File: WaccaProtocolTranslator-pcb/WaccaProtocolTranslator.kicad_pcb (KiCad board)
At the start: 2 copper layers, 161.5 x 111 mm, 114 parts, among them IC1 W25Q16JVUXIQ_TR, IC2 W25Q16JVUXIQ_TR, J1 USB_C_Receptacle_USB2.0, J10 Barrel_Jack, J2 6116314-1, J3 USB_C_Receptacle_USB2.0, J4 USB_C_Receptacle_USB2.0, J5 Conn_01x03_Male, J6 Conn_01x03_Male, J7 Conn_02x02_Odd_Even, J8 Conn_01x08_Male, J9 Barrel_Jack, Q1 IRLB8721PBF, Q2 IRLB8721PBF, SW1 Program Left, SW2 Program Right, SW3 Reset, U1 NCP1117-3.3_SOT223, U2 93LCxxB, U3 RP2040, U4 FT232HQ-REEL, U5 RP2040, Y1 ABLS-12.000MHZ-B4-T, Y2 ABLS-12.000MHZ-B4-T, Y3 ABLS-12.000MHZ-B4-T

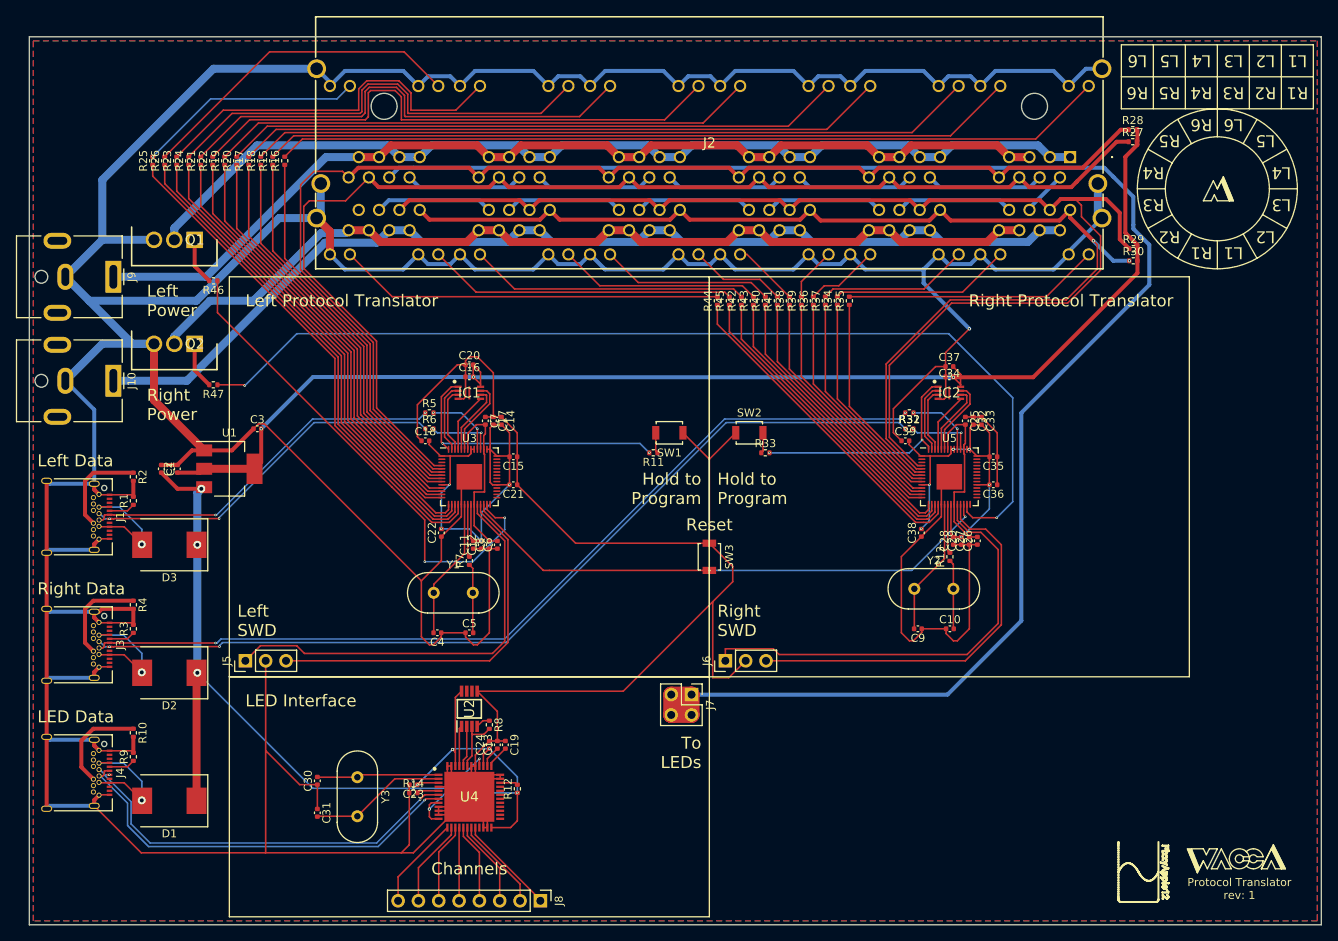
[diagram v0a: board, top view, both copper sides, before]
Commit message: A few changes that needed to be pushed, the power switching circuitry has been removed temporarily to allow for manual power switching. I also baked the FT232HQ connection to the LED bus and changed the Via sizes to match the drilling specs required by most PCB fab services.
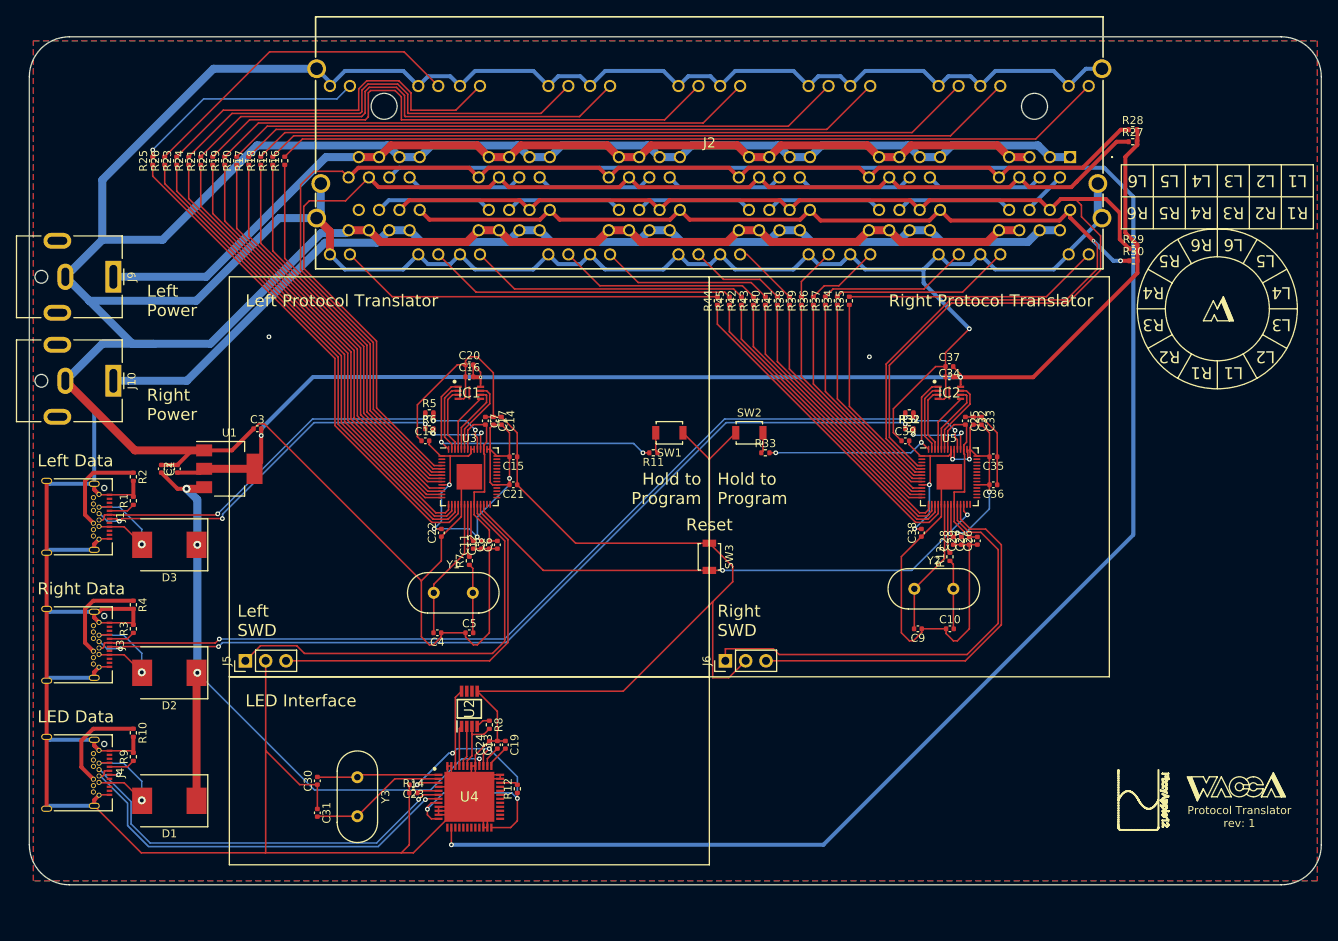
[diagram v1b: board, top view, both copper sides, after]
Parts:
- removed J7: Conn_02x02_Odd_Even, Connector_PinHeader_2.54mm:PinHeader_2x02_P2.54mm_Vertical
- removed J8: Conn_01x08_Male, Connector_PinHeader_2.54mm:PinHeader_1x08_P2.54mm_Vertical
- removed Q1, Q2: IRLB8721PBF, SamacSys_Parts:TO254P483X1016X1994-3P
- removed R46, R47: 275, Resistor_SMD:R_0402_1005Metric
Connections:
- C1 pad 1: Earth -> TP_GND_LEFT
- C10 pad 1: Earth -> TP_GND_LEFT
- C11 pad 1: Earth -> TP_GND_LEFT
- C12 pad 1: Earth -> TP_GND_LEFT
- C13 pad 2: Earth -> TP_GND_LEFT
- C14 pad 1: Earth -> TP_GND_LEFT
- C15 pad 1: Earth -> TP_GND_LEFT
- C16 pad 1: Earth -> TP_GND_LEFT
- C17 pad 1: Earth -> TP_GND_LEFT
- C18 pad 1: Earth -> TP_GND_LEFT
- C19 pad 1: Earth -> TP_GND_LEFT
- C2 pad 2: Earth -> TP_GND_LEFT
- C20 pad 1: Earth -> TP_GND_LEFT
- C21 pad 1: Earth -> TP_GND_LEFT
- C22 pad 1: Earth -> TP_GND_LEFT
- C23 pad 2: Earth -> TP_GND_LEFT
- C24 pad 2: Earth -> TP_GND_LEFT
- C25 pad 1: Earth -> TP_GND_LEFT
- C26 pad 1: Earth -> TP_GND_LEFT
- C27 pad 1: Earth -> TP_GND_LEFT
- C28 pad 1: Earth -> TP_GND_LEFT
- C29 pad 1: Earth -> TP_GND_LEFT
- C3 pad 1: Earth -> TP_GND_LEFT
- C30 pad 1: Earth -> TP_GND_LEFT
- C31 pad 1: Earth -> TP_GND_LEFT
- C32 pad 1: Earth -> TP_GND_LEFT
- C33 pad 1: Earth -> TP_GND_LEFT
- C34 pad 1: Earth -> TP_GND_LEFT
- C35 pad 1: Earth -> TP_GND_LEFT
- C36 pad 1: Earth -> TP_GND_LEFT
- C37 pad 1: Earth -> TP_GND_LEFT
- C38 pad 1: Earth -> TP_GND_LEFT
- C39 pad 1: Earth -> TP_GND_LEFT
- C4 pad 1: Earth -> TP_GND_LEFT
- C5 pad 1: Earth -> TP_GND_LEFT
- C6 pad 1: Earth -> TP_GND_LEFT
- C7 pad 1: Earth -> TP_GND_LEFT
- C8 pad 1: Earth -> TP_GND_LEFT
- C9 pad 1: Earth -> TP_GND_LEFT
- IC1 pad 4: Earth -> TP_GND_LEFT
- IC2 pad 4: Earth -> TP_GND_LEFT
- J1 pad A1: Earth -> TP_GND_LEFT
- J1 pad A12: Earth -> TP_GND_LEFT
- J1 pad B1: Earth -> TP_GND_LEFT
- J1 pad B12: Earth -> TP_GND_LEFT
- J1 pad S1: Earth -> TP_GND_LEFT
- J10 pad 2: Earth -> TP_GND_LEFT
- J2 pad A10: Earth -> TP_GND_LEFT
- J2 pad A12: Earth -> TP_GND_LEFT
- J2 pad B10: Earth -> TP_GND_LEFT
- J2 pad B12: Earth -> TP_GND_LEFT
- J2 pad C10: Earth -> TP_GND_LEFT
- J2 pad C12: Earth -> TP_GND_LEFT
- J2 pad D10: Earth -> TP_GND_LEFT
- J2 pad D12: Earth -> TP_GND_LEFT
- J2 pad E10: Earth -> TP_GND_LEFT
- J2 pad E12: Earth -> TP_GND_LEFT
- J2 pad F10: Earth -> TP_GND_LEFT
- J2 pad F12: Earth -> TP_GND_LEFT
- J2 pad G1: TP_GND_RIGHT -> TP_GND_LEFT
- J2 pad G11: Earth -> TP_GND_LEFT
- J2 pad G3: TP_GND_RIGHT -> TP_GND_LEFT
- J2 pad G9: Earth -> TP_GND_LEFT
- J2 pad H1: TP_GND_RIGHT -> TP_GND_LEFT
- J2 pad H11: Earth -> TP_GND_LEFT
- J2 pad H3: TP_GND_RIGHT -> TP_GND_LEFT
- J2 pad H9: Earth -> TP_GND_LEFT
- J2 pad J1: TP_GND_RIGHT -> TP_GND_LEFT
- J2 pad J11: Earth -> TP_GND_LEFT
- J2 pad J3: TP_GND_RIGHT -> TP_GND_LEFT
- J2 pad J9: Earth -> TP_GND_LEFT
- J2 pad K1: TP_GND_RIGHT -> TP_GND_LEFT
- J2 pad K11: Earth -> TP_GND_LEFT
- J2 pad K3: TP_GND_RIGHT -> TP_GND_LEFT
- J2 pad K9: Earth -> TP_GND_LEFT
- J2 pad L1: TP_GND_RIGHT -> TP_GND_LEFT
- J2 pad L11: Earth -> TP_GND_LEFT
- J2 pad L3: TP_GND_RIGHT -> TP_GND_LEFT
- J2 pad L9: Earth -> TP_GND_LEFT
- J2 pad M1: TP_GND_RIGHT -> TP_GND_LEFT
- J2 pad M11: Earth -> TP_GND_LEFT
- J2 pad M3: TP_GND_RIGHT -> TP_GND_LEFT
- J2 pad M9: Earth -> TP_GND_LEFT
- J2 pad MH1: Earth -> TP_GND_LEFT
- J2 pad MH2: Earth -> TP_GND_LEFT
- J2 pad MH3: Earth -> TP_GND_LEFT
- J2 pad MH4: Earth -> TP_GND_LEFT
- J2 pad MH5: Earth -> TP_GND_LEFT
- J2 pad MH6: Earth -> TP_GND_LEFT
- J3 pad A1: Earth -> TP_GND_LEFT
- J3 pad A12: Earth -> TP_GND_LEFT
- J3 pad B1: Earth -> TP_GND_LEFT
- J3 pad B12: Earth -> TP_GND_LEFT
- J3 pad S1: Earth -> TP_GND_LEFT
- J4 pad A1: Earth -> TP_GND_LEFT
- J4 pad A12: Earth -> TP_GND_LEFT
- J4 pad B1: Earth -> TP_GND_LEFT
- J4 pad B12: Earth -> TP_GND_LEFT
- J4 pad S1: Earth -> TP_GND_LEFT
- J5 pad 2: Earth -> TP_GND_LEFT
- J6 pad 2: Earth -> TP_GND_LEFT
- J9 pad 2: Earth -> TP_GND_LEFT
- R1 pad 2: Earth -> TP_GND_LEFT
- R10 pad 2: Earth -> TP_GND_LEFT
- R14 pad 1: Earth -> TP_GND_LEFT
- R2 pad 2: Earth -> TP_GND_LEFT
- R3 pad 2: Earth -> TP_GND_LEFT
- R4 pad 2: Earth -> TP_GND_LEFT
- R9 pad 2: Earth -> TP_GND_LEFT
- SW1 pad 1: Earth -> TP_GND_LEFT
- SW2 pad 1: Earth -> TP_GND_LEFT
- SW3 pad 1: Earth -> TP_GND_LEFT
- U1 pad 1: Earth -> TP_GND_LEFT
- U2 pad 5: Earth -> TP_GND_LEFT
- U3 pad 19: Earth -> TP_GND_LEFT
- U3 pad 27: POWER_SWITCH_LEFT -> unconnected-(U3-GPIO16-Pad27)
- U3 pad 57: Earth -> TP_GND_LEFT
- U4 pad 10: Earth -> TP_GND_LEFT
- U4 pad 11: Earth -> TP_GND_LEFT
- U4 pad 13: LED_TCK -> unconnected-(U4-ADBUS0-Pad13)
- U4 pad 14: LED_TDI -> TPL6_LED_IN
- U4 pad 15: LED_TDO -> unconnected-(U4-ADBUS2-Pad15)
- U4 pad 16: LED_TMS -> unconnected-(U4-ADBUS3-Pad16)
- U4 pad 17: LED_GP0 -> unconnected-(U4-ADBUS4-Pad17)
- U4 pad 18: LED_GP1 -> unconnected-(U4-ADBUS5-Pad18)
- U4 pad 19: LED_GP2 -> unconnected-(U4-ADBUS6-Pad19)
- U4 pad 20: LED_GP3 -> unconnected-(U4-ADBUS7-Pad20)
- U4 pad 22: Earth -> TP_GND_LEFT
- U4 pad 23: Earth -> TP_GND_LEFT
- U4 pad 35: Earth -> TP_GND_LEFT
- U4 pad 36: Earth -> TP_GND_LEFT
- U4 pad 4: Earth -> TP_GND_LEFT
- U4 pad 41: Earth -> TP_GND_LEFT
- U4 pad 42: Earth -> TP_GND_LEFT
- U4 pad 47: Earth -> TP_GND_LEFT
- U4 pad 48: Earth -> TP_GND_LEFT
- U4 pad 49: Earth -> TP_GND_LEFT
- U4 pad 9: Earth -> TP_GND_LEFT
- U5 pad 19: Earth -> TP_GND_LEFT
- U5 pad 27: POWER_SWITCH_RIGHT -> unconnected-(U5-GPIO16-Pad27)
- U5 pad 57: Earth -> TP_GND_LEFT
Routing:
- net TP_GND_LEFT: track 124.4 -> 1245.0 mm, vias 0 -> 3
- net Earth: track 993.8 -> 0.00 mm, vias 1 -> 0
- net POWER_SWITCH_RIGHT: track 126.3 -> 0.00 mm, vias 2 -> 0
- net TP_GND_RIGHT: track 118.1 -> 0.00 mm
- net POWER_SWITCH_LEFT: track 62.3 -> 0.00 mm, vias 2 -> 0
- net TPL6_LED_IN: track 214.3 -> 240.7 mm, vias 0 -> 1
- net LED_GP3: track 12.5 -> 0.00 mm
- net LED_TCK: track 11.7 -> 0.00 mm
- net LED_GP2: track 11.7 -> 0.00 mm
- net LED_TDI: track 10.9 -> 0.00 mm
- net LED_GP1: track 10.8 -> 0.00 mm
- net LED_TDO: track 10.0 -> 0.00 mm
- net LED_GP0: track 9.98 -> 0.00 mm
- net LED_TMS: track 9.16 -> 0.00 mm
- net Net-(U5-ADC_AVDD): track 50.0 -> 56.5 mm
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- added copper zone on B.Cu, net TP_GND_LEFT
- added copper zone on F.Cu, net TP_GND_LEFT
- removed copper zone on B.Cu, net Earth
- removed copper zone on F.Cu, net Earth
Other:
- board size 161.5 x 111 mm -> 161.5 x 106 mm
- board text removed: "Channels"
- board text removed: "To LEDs"
